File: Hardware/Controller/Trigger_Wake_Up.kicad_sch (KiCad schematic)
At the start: 25 parts, among them J3 Conn_01x02_Male, Q1 BC818, Q2 AO3401A, Q3 BC818, U6 MCP73811T-420I-OT, X1 CON_JST_PH_2PIN_MTPH2, X2 CON_JST_PH_2PIN_MTPH2

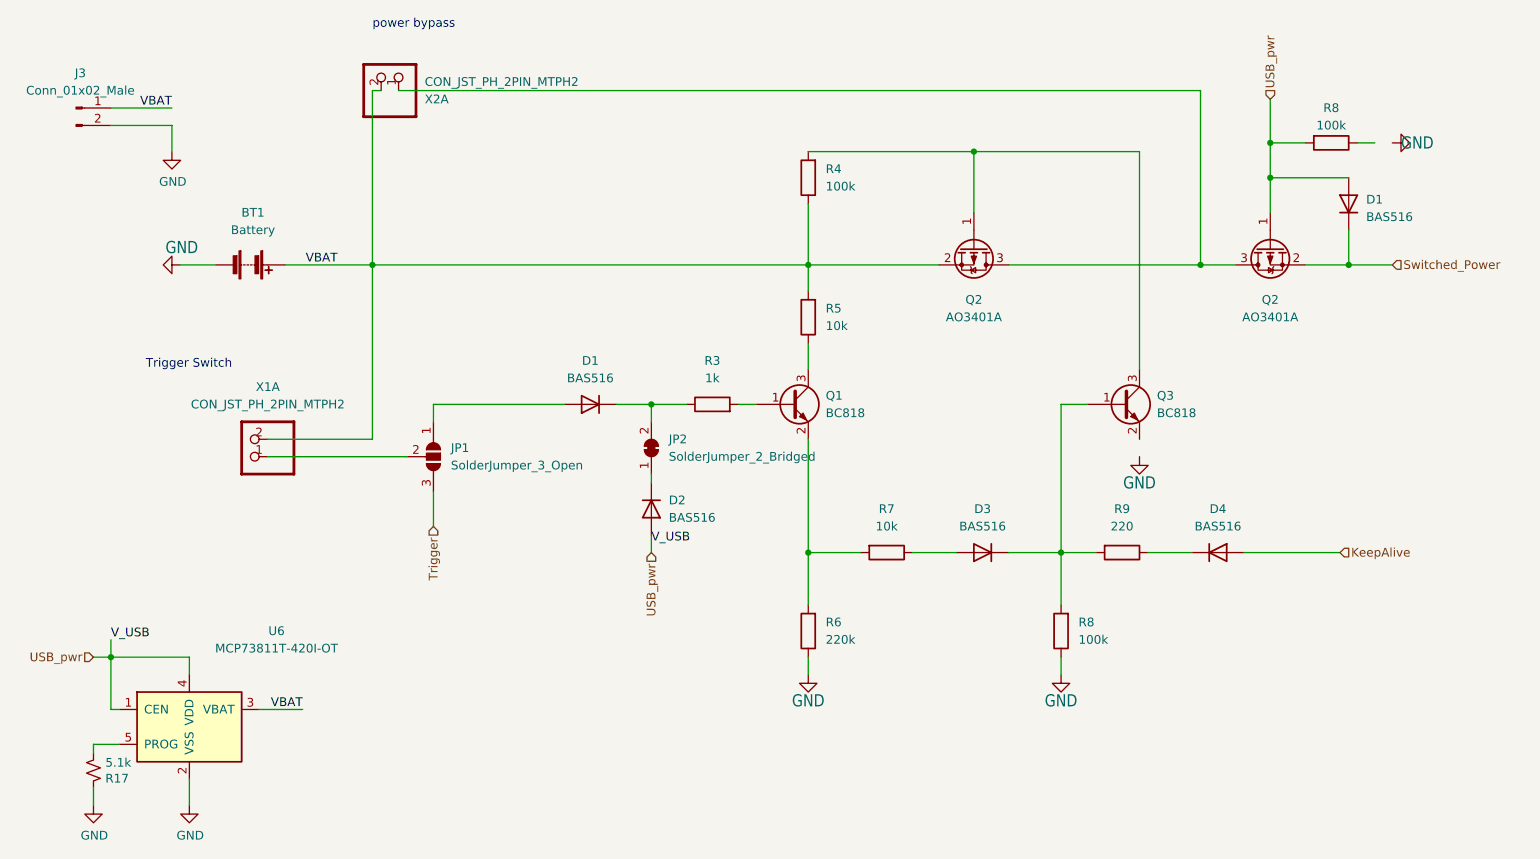
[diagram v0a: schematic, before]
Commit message: added footprint for MTSM2601SMF1-100
Signed-off-by: lokimetasmith <lokimail@gmail.com>
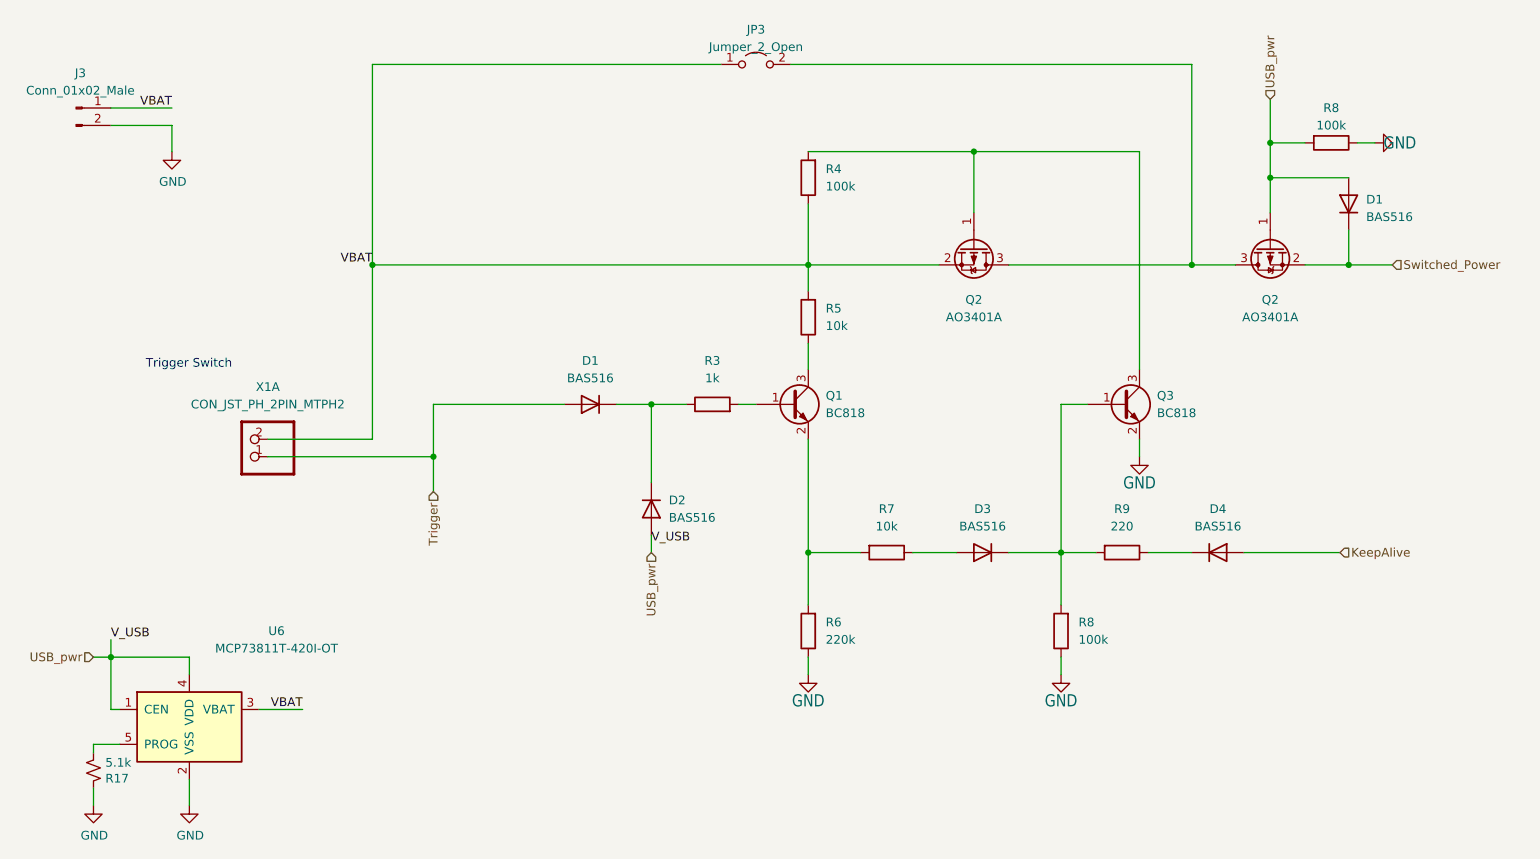
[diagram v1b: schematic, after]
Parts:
- removed BT1: Battery, Battery:BatteryHolder_Keystone_2460_1xAA, symbol Device:Battery
- removed JP1: SolderJumper_3_Open, Jumper:SolderJumper-3_P1.3mm_Open_Pad1.0x1.5mm_NumberLabels, symbol Jumper:SolderJumper_3_Open
- removed JP2: SolderJumper_2_Bridged, Jumper:SolderJumper-2_P1.3mm_Bridged_Pad1.0x1.5mm, symbol Jumper:SolderJumper_2_Bridged
- removed X2: CON_JST_PH_2PIN_MTPH2, Connector_JST:JST_EH_B2B-EH-A_1x02_P2.50mm_Vertical, symbol ControllerBoard-eagle-import:CON_JST_PH_2PIN_MTPH2
- added JP3: Jumper_2_Open, symbol Jumper:Jumper_2_Open
- R3, R4, R5, R6, R7, R8, R9: footprint Resistor_SMD:R_0603_1608Metric_Pad0.98x0.95mm_HandSolder -> Resistor_SMD:R_0402_1005Metric
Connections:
- net GND: now also Q3.2 (E), R8.1
- net Trigger: now also D1.2 (A), X1.1
- net VBAT: now also JP3.1 (A)
- net at D1.1 (K), R3.1: now also D2.1 (K)
- net at Q2.3 (D), Q2.3 (D): now also JP3.2 (B)
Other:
- note removed: "power bypass"

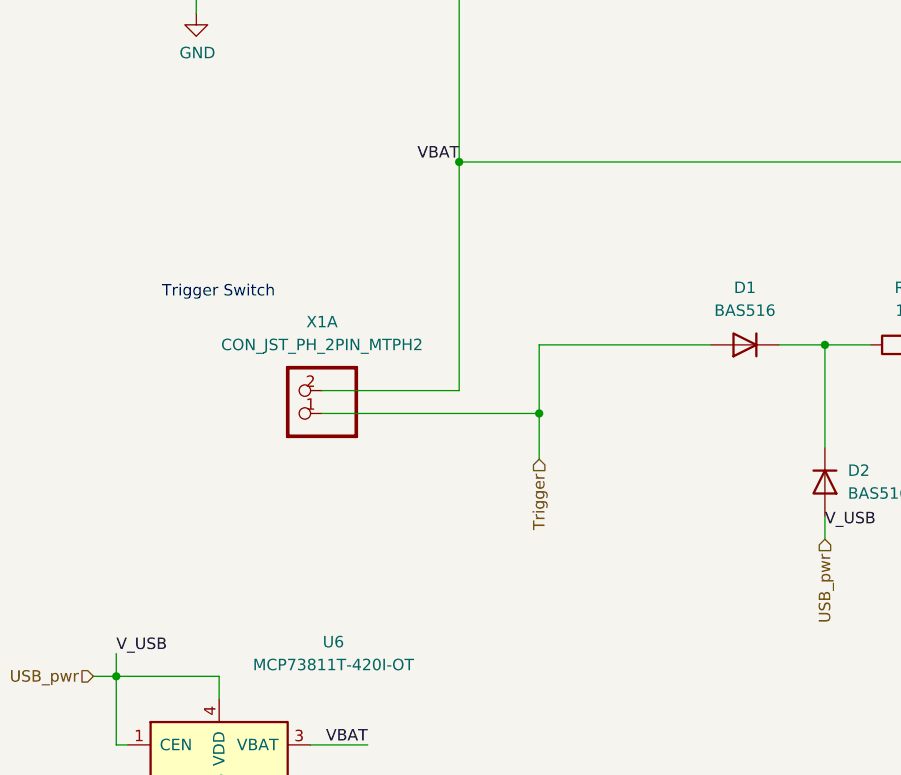
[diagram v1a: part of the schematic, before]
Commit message: as ordered 11/27/2023 from JLCPCB
Updated silk on RoundScanner, minor changes,

major changes on control board, cleaned up foot prints, nudged parts around
control board not ready for release yet
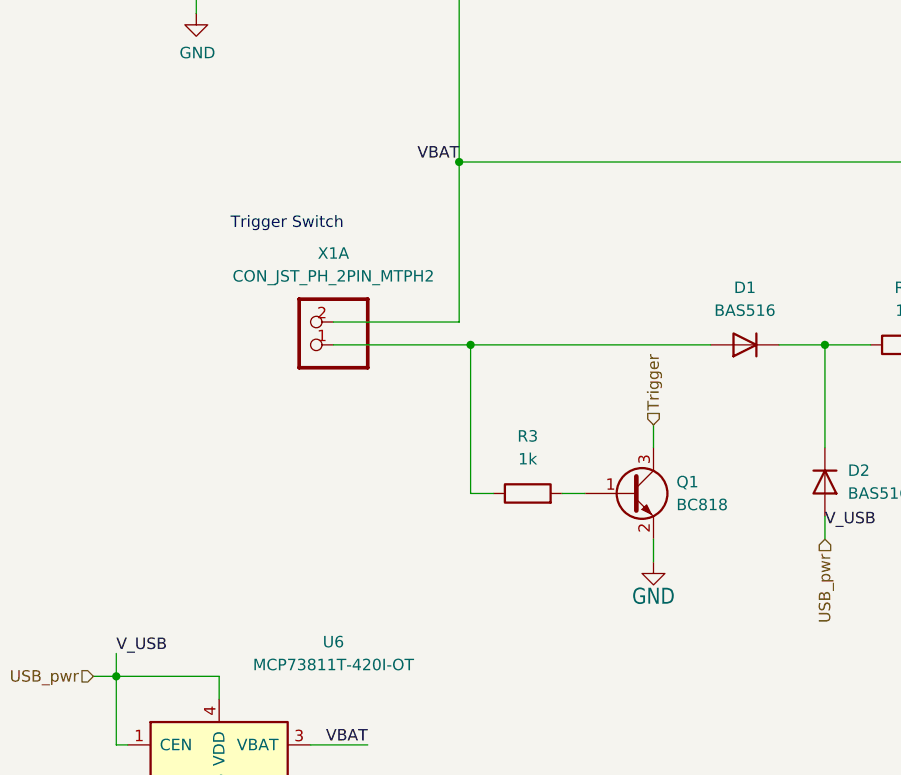
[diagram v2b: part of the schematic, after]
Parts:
- added Q1: BC818, Package_TO_SOT_SMD:SOT-23, symbol Transistor_BJT:BC818
- added R3: 1k, Resistor_SMD:R_0402_1005Metric, symbol Device:R
- JP3: footprint (none) -> Jumper:SolderJumper-2_P1.3mm_Bridged2Bar_RoundedPad1.0x1.5mm
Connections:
- net GND: now also Q1.2 (E)
- net Trigger: now also Q1.3 (C); no longer D1.2 (A), X1.1
- new net: D1.2 (A), R3.1, X1.1
- new net: Q1.1 (B), R3.2
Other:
- moved on the sheet: X1A
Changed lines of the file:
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@@
   (junction (at 187.96 115.57) (diameter 0) (color 0 0 0 0)
   )
-  (junction (at 96.52 101.6) (diameter 0) (color 0 0 0 0)
-  )
   (junction (at 151.13 115.57) (diameter 0) (color 0 0 0 0)
   )
@@
   (junction (at 49.53 130.81) (diameter 0) (color 0 0 0 0)
   )
+  (junction (at 88.9 93.98) (diameter 0) (color 0 0 0 0)
+  )
   (junction (at 175.26 57.15) (diameter 0) (color 0 0 0 0)
   )
-  (wire (pts (xy 87.63 73.66) (xy 87.63 99.06))
-    (stroke (width 0) (type default))
-  )
-  (wire (pts (xy 96.52 93.98) (xy 115.57 93.98))
+  (wire (pts (xy 87.63 73.66) (xy 87.63 91.44))
     (stroke (width 0) (type default))
   )
@@
     (stroke (width 0) (type default))
   )
-  (wire (pts (xy 96.52 93.98) (xy 96.52 101.6))
-    (stroke (width 0) (type default))
-  )
   (wire (pts (xy 87.63 73.66) (xy 151.13 73.66))
     (stroke (width 0) (type default))
@@
     (stroke (width 0) (type default))
   )
+  (wire (pts (xy 88.9 93.98) (xy 88.9 110.49))
+    (stroke (width 0) (type default))
+  )
   (wire (pts (xy 151.13 115.57) (xy 151.13 123.19))
     (stroke (width 0) (type default))
@@
     (stroke (width 0) (type default))
   )
-  (wire (pts (xy 96.52 106.68) (xy 96.52 101.6))
+  (wire (pts (xy 109.22 102.87) (xy 109.22 105.41))
     (stroke (width 0) (type default))
   )
@@
     (stroke (width 0) (type default))
   )
-  (wire (pts (xy 72.39 101.6) (xy 96.52 101.6))
-    (stroke (width 0) (type default))
-  )
   (wire (pts (xy 60.96 152.4) (xy 60.96 148.59))
     (stroke (width 0) (type default))
@@
     (stroke (width 0) (type default))
   )
+  (wire (pts (xy 88.9 110.49) (xy 91.44 110.49))
+    (stroke (width 0) (type default))
+  )
   (wire (pts (xy 231.14 55.88) (xy 233.68 55.88))
     (stroke (width 0) (type default))
@@
     (stroke (width 0) (type default))
   )
-  (wire (pts (xy 72.39 99.06) (xy 87.63 99.06))
+  (wire (pts (xy 73.66 91.44) (xy 87.63 91.44))
     (stroke (width 0) (type default))
   )
@@
     (stroke (width 0) (type default))
   )
+  (wire (pts (xy 73.66 93.98) (xy 88.9 93.98))
+    (stroke (width 0) (type default))
+  )
+  (wire (pts (xy 109.22 115.57) (xy 109.22 118.11))
+    (stroke (width 0) (type default))
+  )
   (wire (pts (xy 140.97 93.98) (xy 143.51 93.98))
     (stroke (width 0) (type default))
@@
     (stroke (width 0) (type default))
   )
+  (wire (pts (xy 88.9 93.98) (xy 115.57 93.98))
+    (stroke (width 0) (type default))
+  )
   (wire (pts (xy 60.96 130.81) (xy 49.53 130.81))
     (stroke (width 0) (type default))
@@
     (stroke (width 0) (type default))
   )
+  (wire (pts (xy 99.06 110.49) (xy 101.6 110.49))
+    (stroke (width 0) (type default))
+  )
   (wire (pts (xy 187.96 93.98) (xy 187.96 115.57))
     (stroke (width 0) (type default))
@@
     (stroke (width 0) (type default))
   )
-  (text "Trigger Switch" (at 54.61 88.9 0)
+  (text "Trigger Switch" (at 62.23 81.28 0)
     (effects (font (size 1.27 1.27)) (justify left bottom))
   )
@@
     (effects (font (size 1.27 1.27)) (justify left))
   )
-  (hierarchical_label "Trigger" (shape input) (at 96.52 106.68 270) (fields_autoplaced)
-    (effects (font (size 1.27 1.27)) (justify right))
-    (property "Intersheetrefs" "${INTERSHEET_REFS}" (at 96.5994 115.6245 90)
-      (effects (font (size 1.27 1.27)) (justify right) hide)
+  (hierarchical_label "Trigger" (shape input) (at 109.22 102.87 90) (fields_autoplaced)
+    (effects (font (size 1.27 1.27)) (justify left))
+    (property "Intersheetrefs" "${INTERSHEET_REFS}" (at 109.22 94.1953 90)
+      (effects (font (size 1.27 1.27)) (justify left) hide)
     )
   )
@@
     )
   )
+  (symbol (lib_id "power:GND") (at 109.22 118.11 0) (unit 1)
+    (in_bom yes) (on_board yes) (dnp no) (fields_autoplaced)
+    (property "Reference" "#GND01" (at 109.22 118.11 0)
+      (effects (font (size 1.27 1.27)) hide)
+    )
+    (property "Value" "GND" (at 109.22 121.92 0)
+      (effects (font (size 1.778 1.5113)))
+    )
+    (property "Footprint" "ControllerBoard:" (at 109.22 118.11 0)
+      (effects (font (size 1.27 1.27)) hide)
+    )
+    (property "Datasheet" "" (at 109.22 118.11 0)
+      (effects (font (size 1.27 1.27)) hide)
+    )
+    (pin "1")
+    (instances
+      (project "ControllerBoard"
+        (path "/87b8a818-7e02-4010-87ed-f48f8c369cfd"
+          (reference "#GND01") (unit 1)
+        )
+        (path "/87b8a818-7e02-4010-87ed-f48f8c369cfd/47976023-e8b5-4c8c-86a2-67e80dfa18fe"
+          (reference "#GND01") (unit 1)
+        )
+      )
+    )
+  )
   (symbol (lib_id "Device:R") (at 162.56 115.57 270) (unit 1)
     (in_bom yes) (on_board yes) (dnp no) (fields_autoplaced)
@@
       (effects (font (size 1.27 1.27)))
     )
-    (property "Footprint" "" (at 143.51 44.45 0)
+    (property "Footprint" "Jumper:SolderJumper-2_P1.3mm_Bridged2Bar_RoundedPad1.0x1.5mm" (at 143.51 44.45 0)
       (effects (font (size 1.27 1.27)) hide)
     )
@@
     )
   )
-  (symbol (lib_id "ControllerBoard-eagle-import:CON_JST_PH_2PIN_MTPH2") (at 69.85 99.06 180) (unit 1)
-    (in_bom yes) (on_board yes) (dnp no) (fields_autoplaced)
-    (property "Reference" "X1" (at 72.39 91.44 0)
-      (effects (font (size 1.27 1.27)))
-    )
-    (property "Value" "CON_JST_PH_2PIN_MTPH2" (at 72.39 93.98 0)
-      (effects (font (size 1.27 1.27)))
-    )
-    (property "Footprint" "Connector_JST:JST_EH_B2B-EH-A_1x02_P2.50mm_Vertical" (at 69.85 99.06 0)
-      (effects (font (size 1.27 1.27)) hide)
-    )
-    (property "Datasheet" "" (at 69.85 99.06 0)
+  (symbol (lib_id "ControllerBoard-eagle-import:CON_JST_PH_2PIN_MTPH2") (at 71.12 91.44 180) (unit 1)
+    (in_bom yes) (on_board yes) (dnp no) (fields_autoplaced)
+    (property "Reference" "X1" (at 73.66 83.82 0)
+      (effects (font (size 1.27 1.27)))
+    )
+    (property "Value" "CON_JST_PH_2PIN_MTPH2" (at 73.66 86.36 0)
+      (effects (font (size 1.27 1.27)))
+    )
+    (property "Footprint" "Connector_JST:JST_EH_B2B-EH-A_1x02_P2.50mm_Vertical" (at 71.12 91.44 0)
+      (effects (font (size 1.27 1.27)) hide)
+    )
+    (property "Datasheet" "" (at 71.12 91.44 0)
       (effects (font (size 1.27 1.27)) hide)
     )
@@
         (path "/87b8a818-7e02-4010-87ed-f48f8c369cfd/47976023-e8b5-4c8c-86a2-67e80dfa18fe"
           (reference "D3") (unit 1)
+        )
+      )
+    )
+  )
+  (symbol (lib_id "Transistor_BJT:BC818") (at 106.68 110.49 0) (unit 1)
+    (in_bom yes) (on_board yes) (dnp no) (fields_autoplaced)
+    (property "Reference" "Q1" (at 111.76 109.2199 0)
+      (effects (font (size 1.27 1.27)) (justify left))
+    )
+    (property "Value" "BC818" (at 111.76 111.7599 0)
+      (effects (font (size 1.27 1.27)) (justify left))
+    )
+    (property "Footprint" "Package_TO_SOT_SMD:SOT-23" (at 111.76 112.395 0)
+      (effects (font (size 1.27 1.27) italic) (justify left) hide)
+    )
+    (property "Datasheet" "https://www.onsemi.com/pub/Collateral/BC818-D.pdf" (at 106.68 110.49 0)
+      (effects (font (size 1.27 1.27)) (justify left) hide)
+    )
+    (pin "1")
+    (pin "2")
+    (pin "3")
+    (instances
+      (project "ControllerBoard"
+        (path "/87b8a818-7e02-4010-87ed-f48f8c369cfd"
+          (reference "Q1") (unit 1)
+        )
+        (path "/87b8a818-7e02-4010-87ed-f48f8c369cfd/47976023-e8b5-4c8c-86a2-67e80dfa18fe"
+          (reference "Q5") (unit 1)
         )
       )
@@
         )
       )
+    )
+  )
+  (symbol (lib_id "Device:R") (at 95.25 110.49 90) (unit 1)
+    (in_bom yes) (on_board yes) (dnp no) (fields_autoplaced)
+    (property "Reference" "R3" (at 95.25 104.14 90)
+      (effects (font (size 1.27 1.27)))
+    )
+    (property "Value" "1k" (at 95.25 106.68 90)
+      (effects (font (size 1.27 1.27)))
+    )
+    (property "Footprint" "Resistor_SMD:R_0402_1005Metric" (at 95.25 112.268 90)
+      (effects (font (size 1.27 1.27)) hide)
+    )
+    (property "Datasheet" "~" (at 95.25 110.49 0)
+      (effects (font (size 1.27 1.27)) hide)
+    )
+    (pin "1")
+    (pin "2")
+    (instances
+      (project "ControllerBoard"
+        (path "/87b8a818-7e02-4010-87ed-f48f8c369cfd"
+          (reference "R3") (unit 1)
+        )
+        (path "/87b8a818-7e02-4010-87ed-f48f8c369cfd/47976023-e8b5-4c8c-86a2-67e80dfa18fe"
+          (reference "R20") (unit 1)
+        )
+      )
